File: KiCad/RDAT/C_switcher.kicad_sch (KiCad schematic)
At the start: 11 parts, among them J18 USB_C_Receptacle_USB2.0, U10 CH224Q

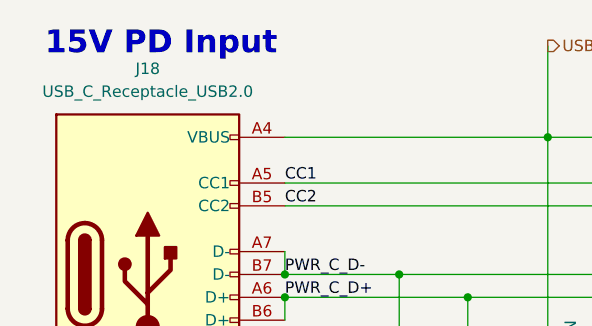
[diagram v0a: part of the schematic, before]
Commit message: Connected m.2 E Key
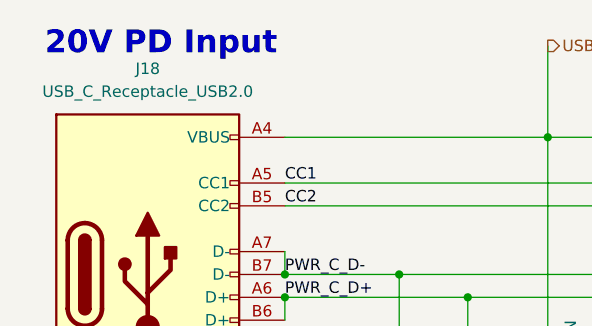
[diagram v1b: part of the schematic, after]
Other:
- note added: "20V PD Input"
- note removed: "15V PD Input"
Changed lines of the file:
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@@
 		)
 	)
-	(text "15V PD Input"
+	(text "20V PD Input"
 		(exclude_from_sim no)
 		(at 45.72 29.21 0)
@@
 			"AFkAAABqAAAAZwAAAEEAAABBAAAATQAAAEkAAAAyAAAAeAAAAEcAAAB5AAAANAAAADgAAAArAAAA"
 			"YwAAAFQAAABrAAAAaQAAAFMAAABDAAAAOAAAAE4AAABEAAAARgAAAGsAAAB0AAAANwAAAGUAAABw"
-			"AAAARgAAAEkAAABLAAAAcQAAAGoAAABWAAAAaAAAADUAAABNAA=="
-		)
-	)
+			"AAAARgAAAEkAAABLAAAAcQAAAGoAAABWAAAAaAAAADUAAABNAHQgS3Vyc2l2AAAAAAAAAAAAAAAA"
+			"AADlz/H5AJQCgAYAAAAQAAAAcMH7//////8AAAAAAAAAAOfP8/kAlQKAVGVybWluYWwAAAAAAAAA"
+			"AAAAAAAAAAAA6c/9+QCWAoBQb2dydWJpb25hIGt1cnN5d2EAAAAAAADrz//5AJcCgAAAAAAAAAAA"
+			"kxay2QAAAACgobvQawEAAO3P+fkAmAKABgAAABAAAADQz/v//////wAAAAAAAAAA78/7+QCZAoAA"
+			"AAAAAAAAAAQ2j9kAAAAA4KC70GsBAACRz4X5AJoCgAYAAAAQAAAAYN37//////8AAAAAAAAAAJPP"
+			"h/kAmwKAAAAAAAAAAADLx7PZAAAAAEClu9BrAQAAlc+B+QCcAoAAAAAAAAAAAMMGs9kAAAAAIKO7"
+			"0GsBAACXz4P5AJ0CgE5lZ3JpdG8gSXTDoWxpY28AAAAAAAAAAJnPjfkAngKABgAAABAAAAAA3/v/"
+			"/////wAAAAAAAAAAm8+P+QCfAoBIYWx2ZmV0IEt1cnNpdgAAAAAAAAAAAACdz4n5AKACgFZldCBD"
+			"dXJzaWVmAAAAAAAAAAAAAAAAAJ/Pi/kAoQKAAAAAAAAAAACSFrbZAAAAAGCnu9BrAQAAgc+V+QCi"
+			"AoBHcmFzc2V0dG8gQ29yc2l2bwAAAAAAAACDz5f5AKMCgAYAAAAQAAAAoOL7//////8AAAAAAAAA"
+			"AIXPkfkApAKAS3JlcGtvIHBvxaFldm5vAAAAAAAAAAAAh8+T+QClAoAAAAAAAAAAABM2stkAAAAA"
+			"YKO70GsBAACJz535AKYCgEbDqWxrw7Z2w6lyIGTFkWx0AAAAAAAAAIvPn/kApwKABgAAABAAAADQ"
+			"7fv//////wAAAAAAAAAAjc+Z+QCoAoAAAAAAAAAAAIuWs9kAAAAA4KO70GsBAACPz5v5AKkCgE5l"
+			"Z3JpdGEgQ3Vyc2l2YQAAAAAAAAAAALHPpfkAqgKAVGVybWluYWwAAAAAAAAAAAAAAAAAAAAAs8+n"
+			"+QCrAoAAAAAAAAAAAAv3s9kAAAAAwKa70GsBAAC1z6H5AKwCgAYAAAAQAAAA4Of7//////8AAAAA"
+			"AAAAALfPo/kArQKAS2FsxLFuIMSwdGFsaWsAAAAAAAAAAAAAuc+t+QCuAoBUZXJtaW5hbAAAAAAA"
+			"AAAAAAAAAAAAAAC7z6/5AK8CgAYAAAAQAAAAcMT7//////8AAAAAAAAAAL3PqfkAsAKAAAAAAAAA"
+			"AABiJrXZAAAAAACnu9BrAQAAv8+r+QCxAoAGAAAAEAAAAJDb+///////AAAAAAAAAAChz7X5ALIC"
+			"gFRlcm1pbmFsAAAAAAAAAAAAAAAAAAAAAKPPt/kAswKAAAAAAA=="
+		)
+	)

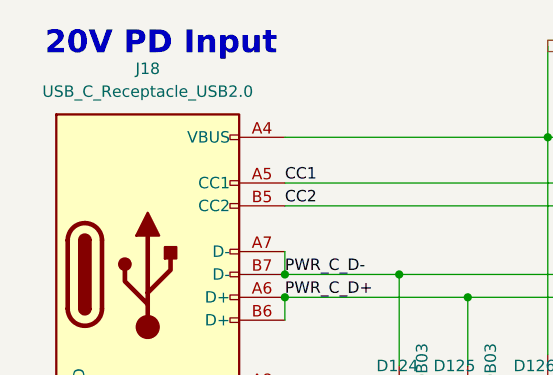
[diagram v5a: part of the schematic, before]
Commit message: Added Libs and DOCS
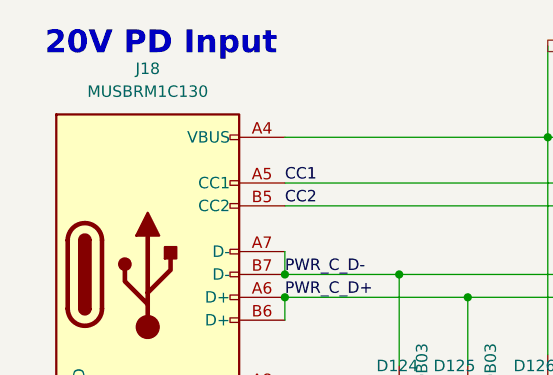
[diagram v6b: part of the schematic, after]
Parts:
- C78: JLCPCB_LINK (none) -> https://jlcpcb.com/partdetail/53938-CL05A105KA5NQNC/C52923
- D124, D125: footprint A_HDJ_Library:D_0402_1005Metric -> Diode_SMD:D_SOD-882; JLCPCB_LINK (none) -> https://jlcpcb.com/partdetail/TechPublic-ESD5V0B031006/C521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
- D126, D127, D128: JLCPCB_LINK (none) -> https://jlcpcb.com/partdetail/Born-PESD24VS1ULN/C406227
- J18: value USB_C_Receptacle_USB2.0 -> MUSBRM1C130; JLCPCB_LINK (none) -> https://www.digikey.com/en/products/detail/amphenol-cs-comm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
- R69: JLCPCB_LINK (none) -> https://jlcpcb.com/partdetail/26487-0402WGF1002TCE/C25744
- R70: JLCPCB_LINK (none) -> https://jlcpcb.com/partdetail/12256-0402WGF1001TCE/C11702
- R71: JLCPCB_LINK (none) -> https://jlcpcb.com/partdetail/26493-0402WGF1203TCE/C25750
- U10: value CH224Q -> CH224K; JLCPCB_LINK (none) -> https://jlcpcb.com/partdetail/wch_jiangsu_Qin_heng-CH224K/C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
